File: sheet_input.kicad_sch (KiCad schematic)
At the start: 45 parts, among them J1 NCJ6FA-H, J5 VDD_PoE / PGND, K1 KAQY214S, K2 KAQY214S, Q1 DMP3098 (P-FET 60V), SW1 SS-12D00-G3, U3 TLV9061, U4 74HC4053

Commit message: feat: expose guitar plug-detect to the carrier on J3.7
Repurpose the dangling PHANTOM_EN line (vestigial since the manual SW1
pivot) as a firmware readback of the guitar-detect signal: J3.7 now
carries DET, so the carrier can see plug state (channel labeling,
muting the mode-switch click).

Instead of the planned 74HCT4053 swap -- no TSSOP-16 HCT4053 exists at
LCSC/JLCPCB from any vendor -- keep the in-stock 74HC4053 (C5648) and
run it from +3V3: VIH drops to 2.31V, so the 3.3V DET drives the select
pins in spec, and the line is native 3.3V for the ESP32-P4's
non-5V-tolerant GPIO. Analog range 0-3.3V covers the codec-bias-centred
signals (worst case ~0.1-2.9V at guitar full-scale); Ron rises
~80->150R, negligible into the codec input.

sheet_input: R19 pull-up, U4 VDD and its decap C29 move +5V -> +3V3
  (U3 buffer stays on +5V for headroom; C25 isolates its bias).
sheet_codec: J3.7 PHANTOM_EN -> DET.
BOM: U4 note updated (part unchanged).

Firmware: configure the J3.7 GPIO as input; low = guitar plugged.
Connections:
- net +3V3: now also C29.1, R19.1, U4.16 (VDD)
- net +5V: no longer C29.1, R19.1, U4.16 (VDD)

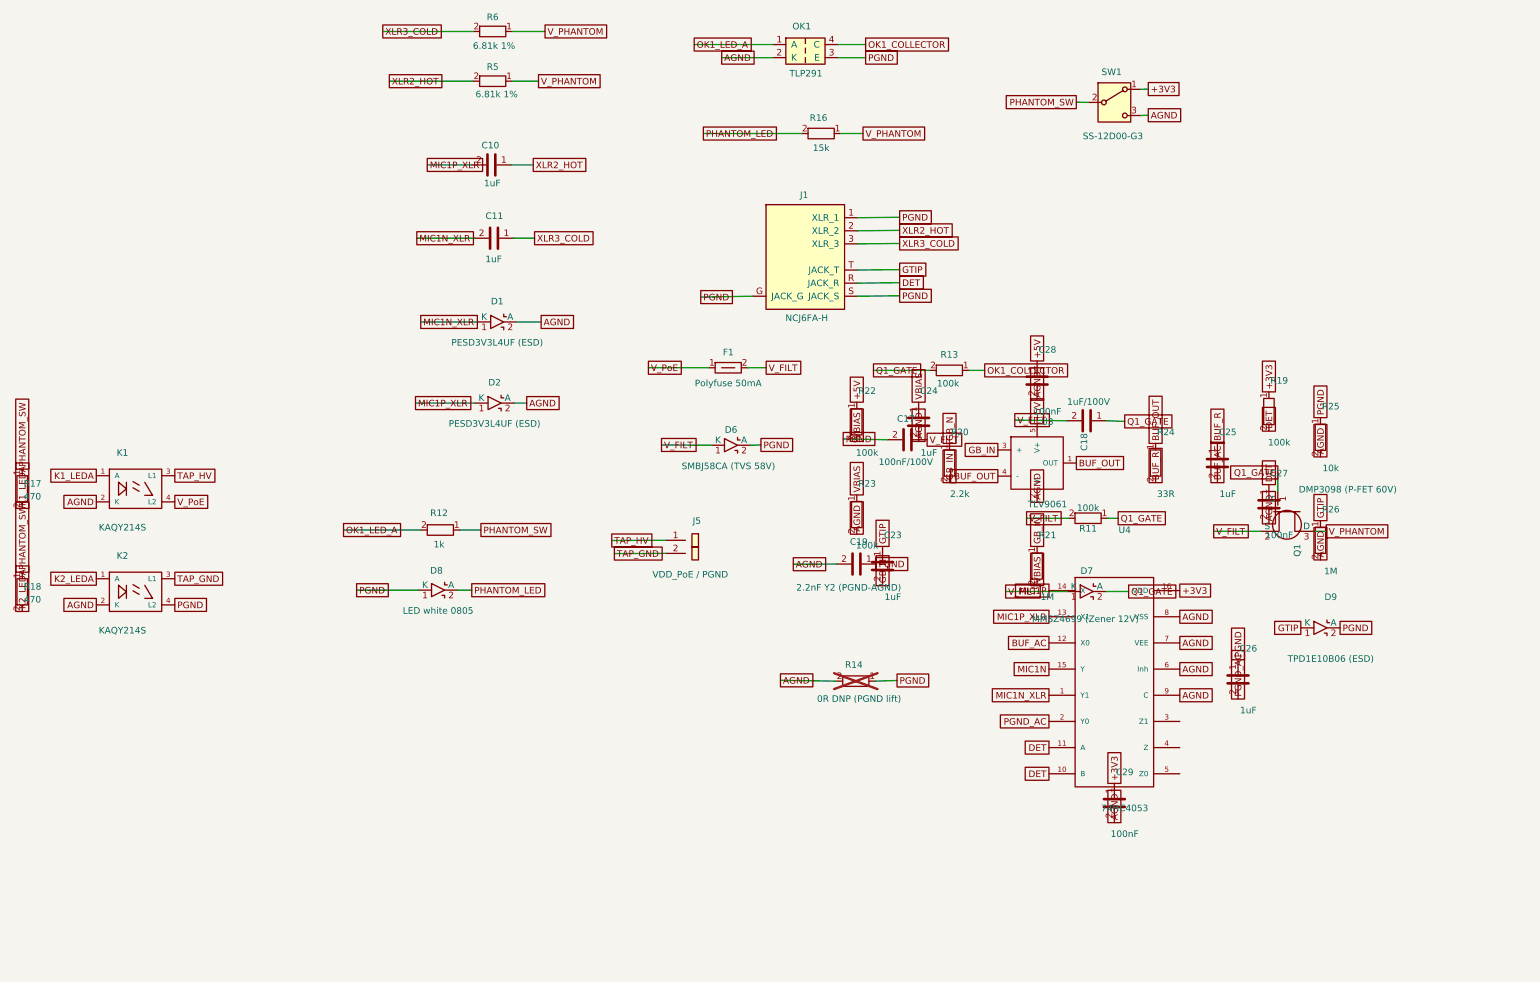
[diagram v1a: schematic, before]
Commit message: cost: D1/D2 ESD swap PESD3V3L4UG -> PESD3V3L1BA-N (C316020)
Only 1 of the 4-line array's channels was in use on each part. The
single-line SOD-323 bidirectional part is a better fit for the mV audio
lines (symmetric clamp, no polarity/orientation for assembly), saves
~$0.14/board at 134k stock, and the 2-pin symbol now matches the part
so the F8 pad-3/4/5 warnings go away. Phantom-transient clamping is
equivalent. Footprint change SOT-353 -> D_SOD-323; re-place at layout.
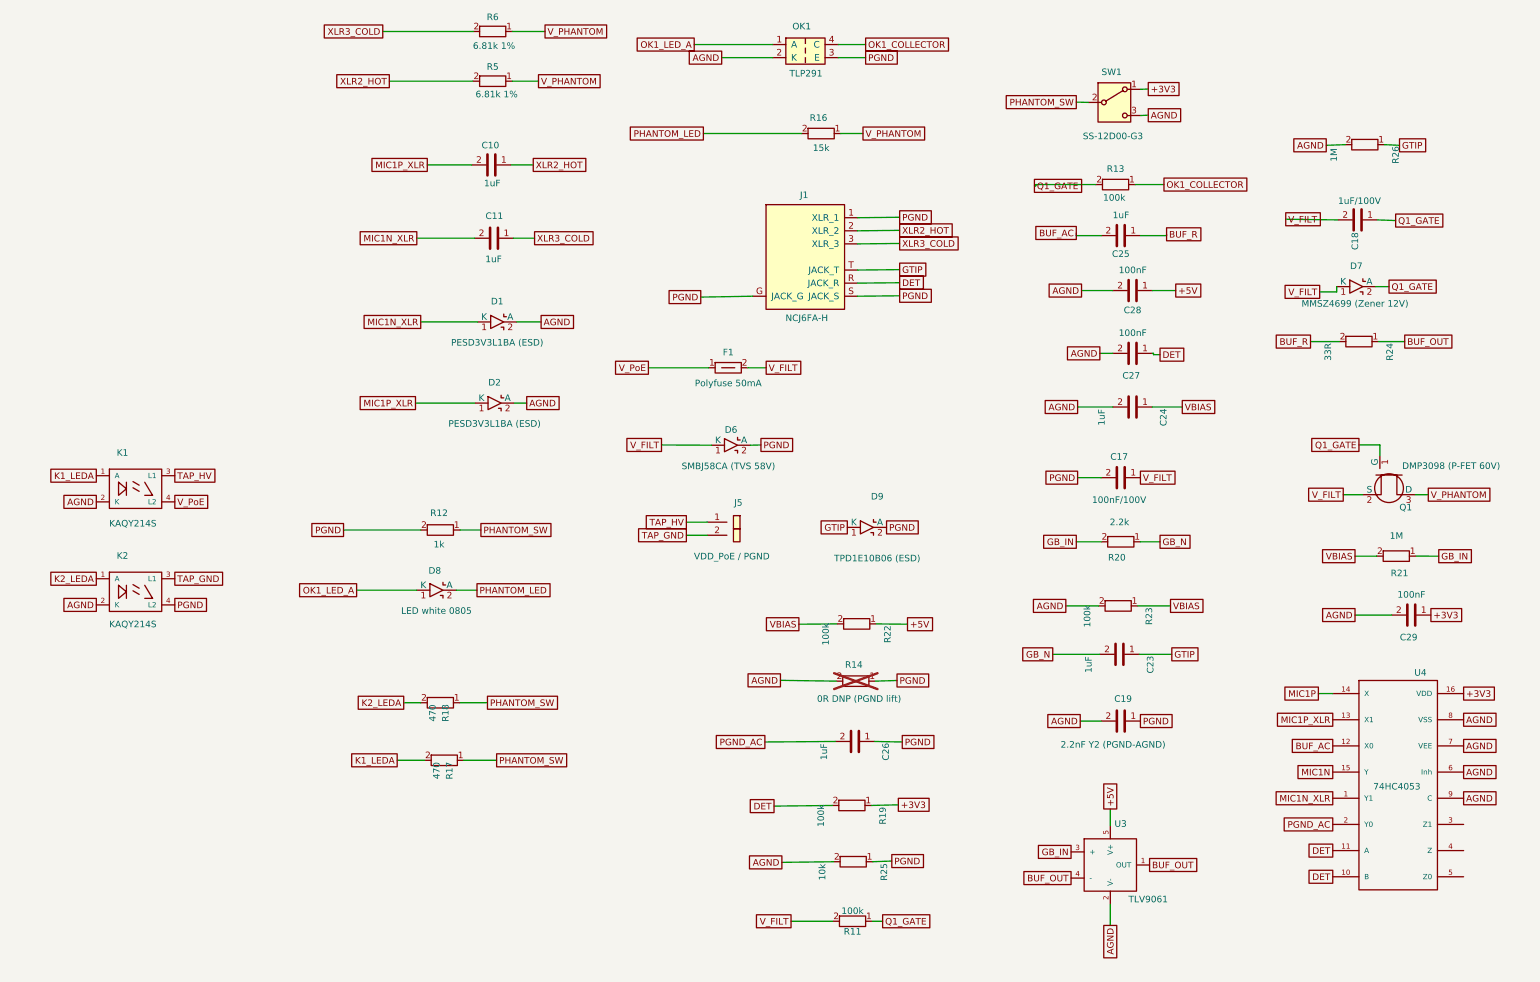
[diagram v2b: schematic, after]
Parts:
- D1, D2: value PESD3V3L4UF (ESD) -> PESD3V3L1BA (ESD); footprint Package_TO_SOT_SMD:SOT-353_SC-70-5 -> Diode_SMD:D_SOD-323
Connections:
- net OK1_LED_A: now also D8.1 (K); no longer R12.2
- net PGND: now also R12.2; no longer D8.1 (K)
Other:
- moved on the sheet: C17, C18, C19, C23, C24, C25, C26, C27, C28, C29, D7, D9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

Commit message: fix: restore D8/R12 phantom-LED wiring swapped during schematic tidy-up
A visual cleanup cross-attached two labels: D8's cathode return picked
up OK1_LED_A while R12's output picked up PGND, putting the opto LED
downstream of the rail it enables (phantom could never start) and
leaving R12 driving ground. Swap the two labels back: R12 -> OK1 LED
anode, D8 -> PGND. Netlist now matches the pre-tidy baseline exactly.
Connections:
- net OK1_LED_A: now also R12.2; no longer D8.1 (K)
- net PGND: now also D8.1 (K); no longer R12.2
